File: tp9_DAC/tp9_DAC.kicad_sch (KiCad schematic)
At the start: 24 parts, among them J2 BAT1, U1 NE555P, U2 NE555P

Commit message: update_tp9_DAC
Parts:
- added H1, H2, H3, H4: MountingHole, MountingHole:MountingHole_2.2mm_M2_DIN965, symbol Mechanical:MountingHole
- added S1, S2: ADE0804, ADE0804:SW_ADE0804, symbol ADE0804:ADE0804
- added TP1, TP2, TP3, TP4, TP5: TestPoint, TestPoint:TestPoint_THTPad_D1.0mm_Drill0.5mm, symbol Connector:TestPoint
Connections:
- net GND: now also C1.2, C10.2, C11.2, C12.2, C2.2, C3.2, C4.2, C5.2, C6.2, C7.2, C8.2, C9.2, TP5.1
- net at C11.1: now also S2.2-1
- net at RL1.1, U1.3 (Q), U2.2 (TR): now also TP1.1
- net at C12.1: now also S2.1-1
- net at RL2.1, U2.3 (Q): now also TP4.1
- net at C7.1: now also S2.6-1
- net at C3.1: now also S1.4-1
- net at RB1.2, U1.2 (TR), U1.6 (THR): now also S1.1, S1.2, S1.3, S1.4, S1.5, S1.6, S1.7, S1.8, TP2.1
- net at C6.1: now also S1.1-1
- net at C8.1: now also S2.5-1
- net at C5.1: now also S1.2-1
- net at RA22.3, U2.6 (THR), U2.7 (DIS): now also S2.1, S2.2, S2.3, S2.4, S2.5, S2.6, S2.7, S2.8, TP3.1
- net at C4.1: now also S1.3-1
- net at C2.1: now also S1.5-1
- net at C10.1: now also S2.3-1
- net at C1.1: now also S1.6-1
- net at C9.1: now also S2.4-1
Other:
- moved on the sheet: C1, C2, C3, C4, C5, C6, J2

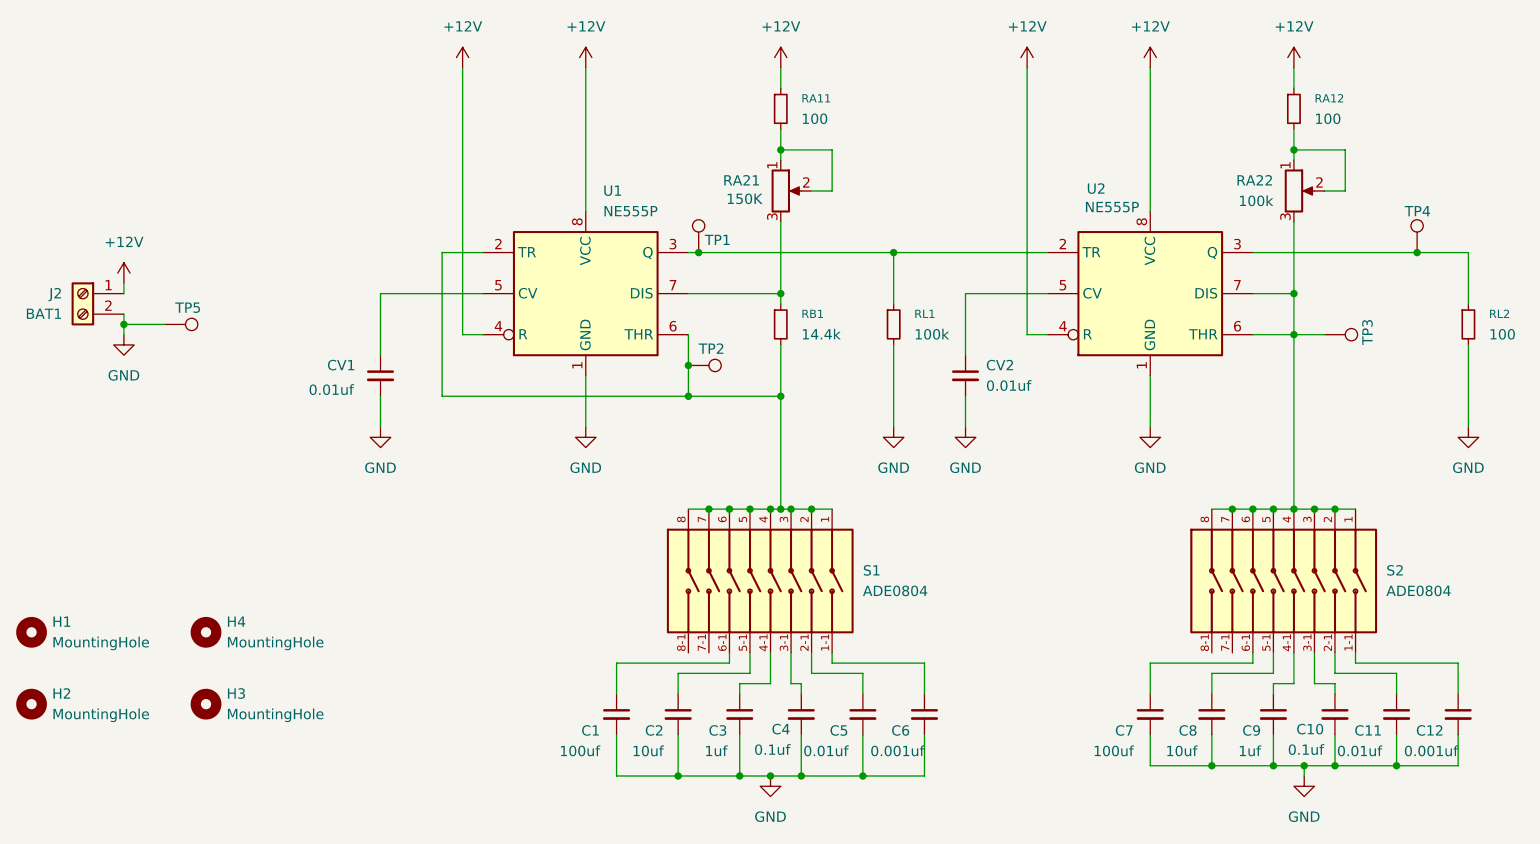
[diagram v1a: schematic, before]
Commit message: update_tp9_pcb
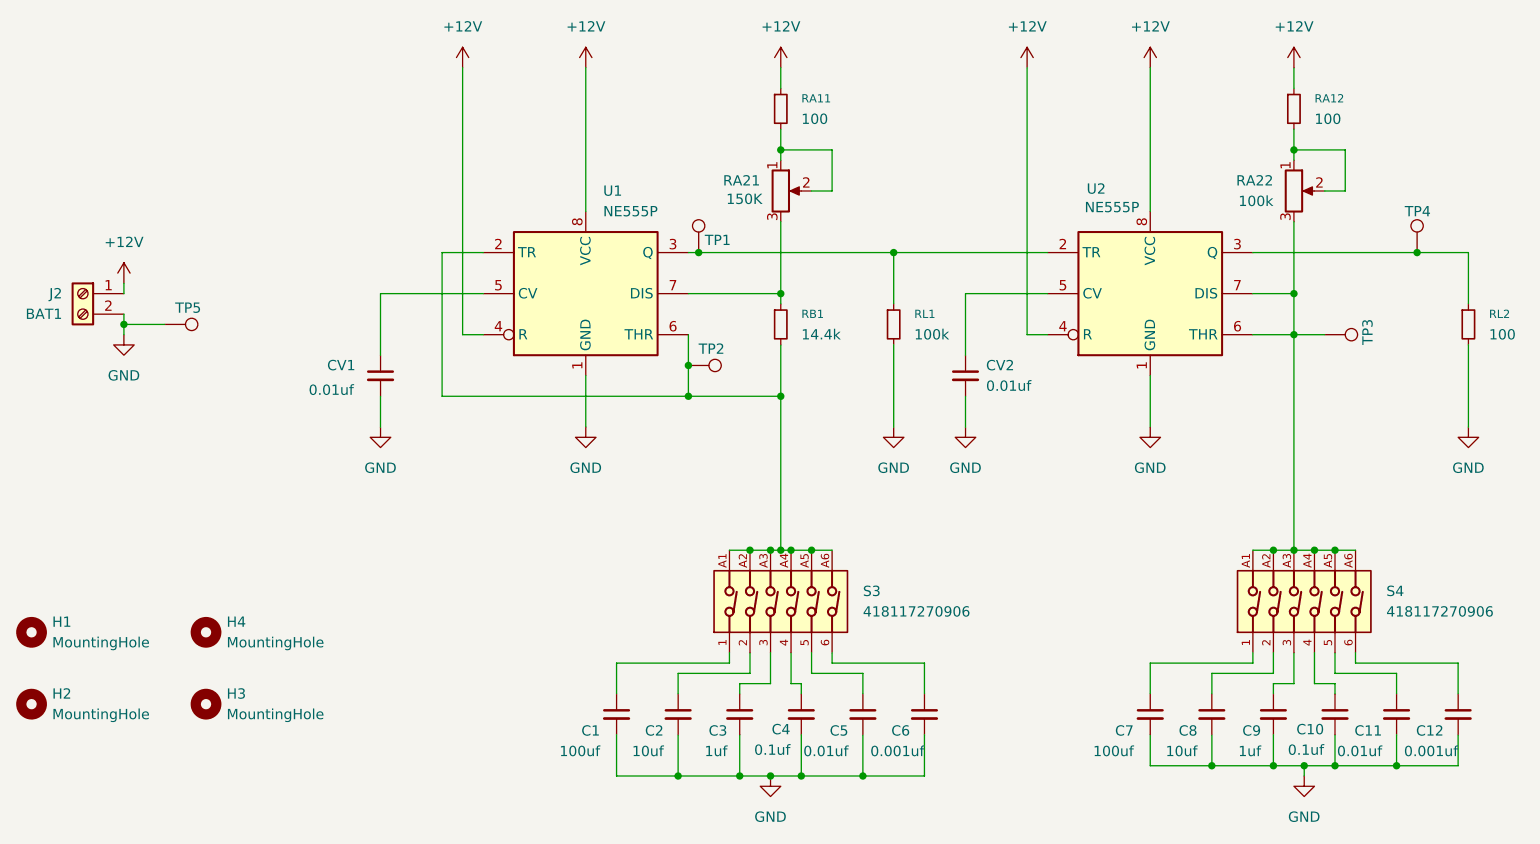
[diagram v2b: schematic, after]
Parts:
- removed S1, S2: ADE0804, ADE0804:SW_ADE0804, symbol ADE0804:ADE0804
- added S3, S4: 418117270906, 418117270906:418117270906, symbol 418117270906:418117270906
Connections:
- net at C10.1: now also S4.4
- net at C8.1: now also S4.2
- net at C11.1: now also S4.5
- net at C3.1: now also S3.3
- net at RB1.2, TP2.1, U1.2 (TR)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: now also S3.A1, S3.A2, S3.A3, S3.A4, S3.A5, S3.A6
- net at C7.1: now also S4.1
- net at C6.1: now also S3.6
- net at C12.1: now also S4.6
- net at C5.1: now also S3.5
- net at RA22.3, TP3.1, U2.6 (THR)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: now also S4.A1, S4.A2, S4.A3, S4.A4, S4.A5, S4.A6
- net at C4.1: now also S3.4
- net at C2.1: now also S3.2
- net at C1.1: now also S3.1
- net at C9.1: now also S4.3
